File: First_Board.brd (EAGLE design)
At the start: 69.8 x 69.8 mm, 61 parts, among them U0 F22X4---DA38, U1 TLC59108PW, U3 A1101, U4 TPS62111RSA

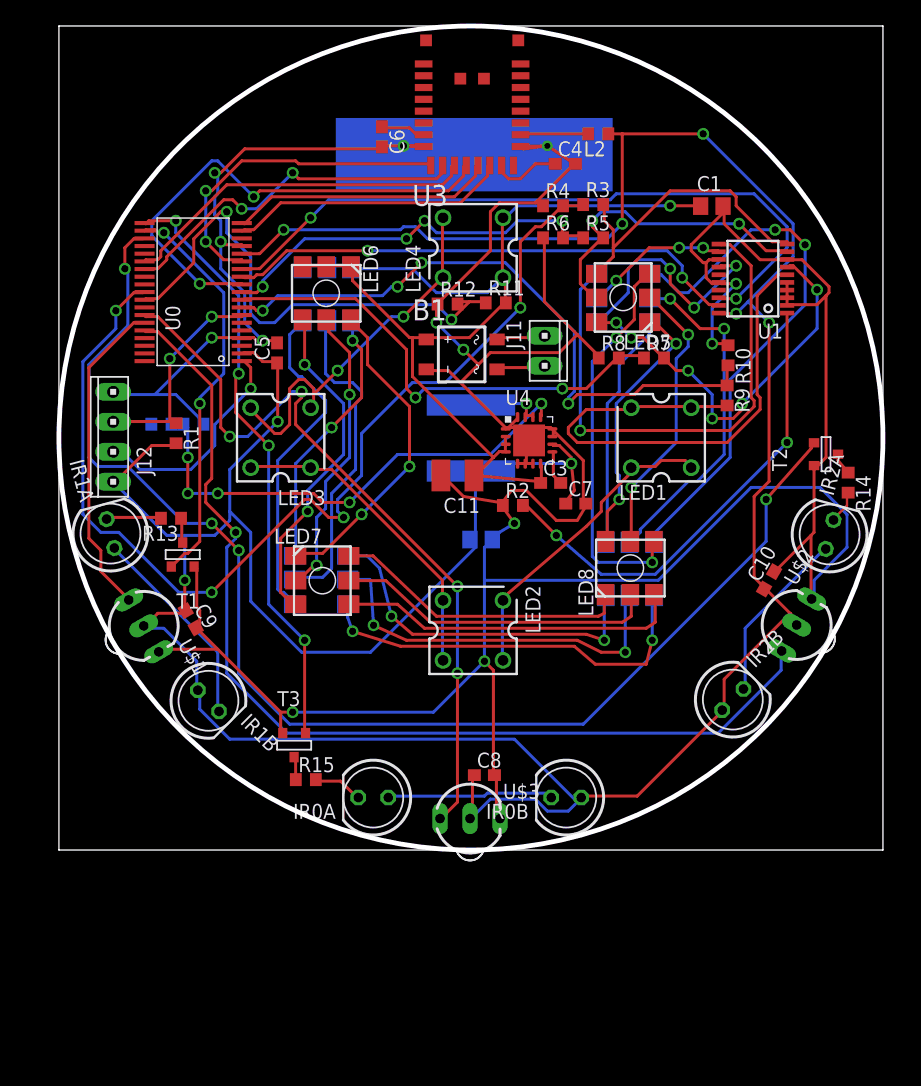
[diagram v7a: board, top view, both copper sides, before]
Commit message: DRC Fixes, moved name labels so they won't overlap exposed copper
git-svn-id: file:///p/svn/Projects/Boards/Driveway_Lights@75 1e7840b9-f7c2-db11-b69c-00d0b71b9132
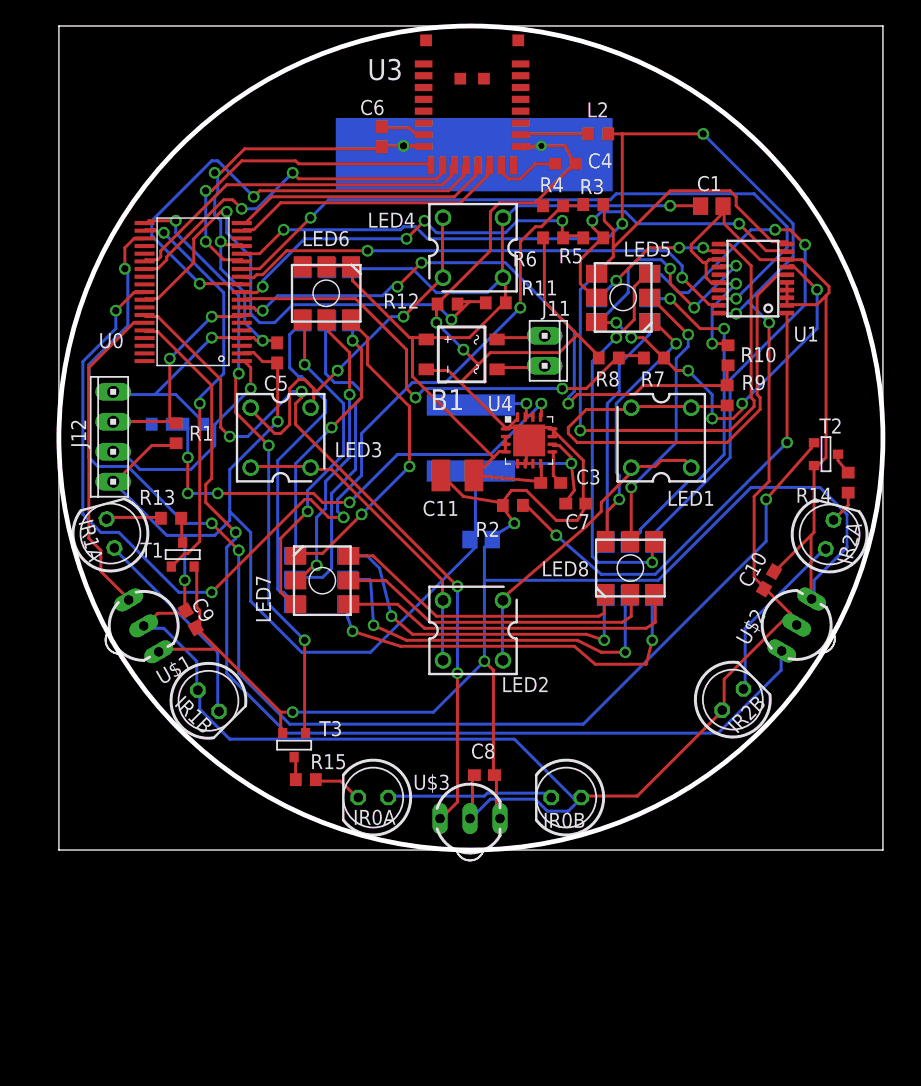
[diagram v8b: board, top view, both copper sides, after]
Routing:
- net GND: track 357.5 -> 357.0 mm
